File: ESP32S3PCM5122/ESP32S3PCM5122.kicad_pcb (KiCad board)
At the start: 2 copper layers, 84 x 70 mm, 28 parts, among them IC1 ESP32-S3-WROOM-1U-N16R8, IC2 AP63203, IC4 USBLC6, J1 OUT, J2 VOL, J5 PWR SW, J6 PWR LED, J7 USB IN, U1 PCM5122PW

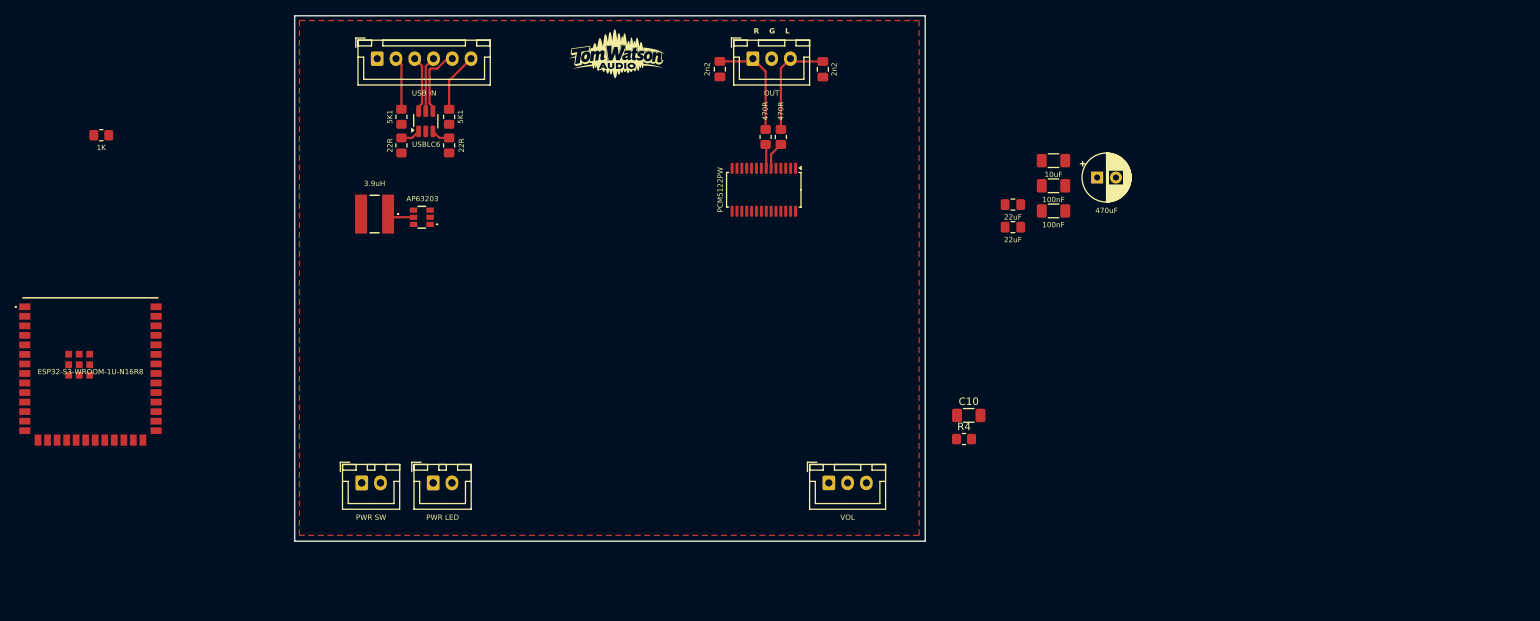
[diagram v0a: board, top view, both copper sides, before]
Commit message: move to PCM5242
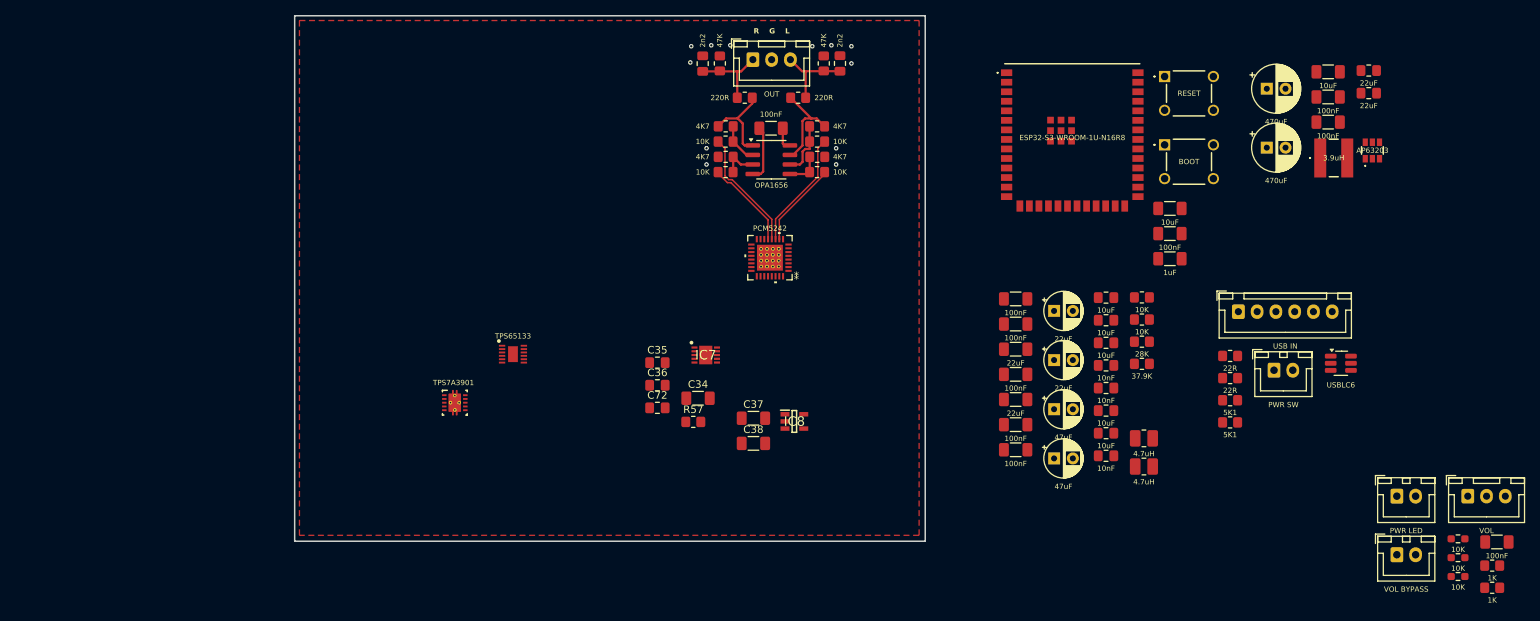
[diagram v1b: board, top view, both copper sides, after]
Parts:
- removed G***: LOGO, Custom:LOGONEW
- added C11: 10uF, Capacitor_SMD:C_1206_3216Metric_Pad1.33x1.80mm_HandSolder, F.Cu at (209.3, 104.4)
- added C12: 100nF, Capacitor_SMD:C_1206_3216Metric_Pad1.33x1.80mm_HandSolder, F.Cu at (209.3, 107.8)
- added C13: 1uF, Capacitor_SMD:C_1206_3216Metric_Pad1.33x1.80mm_HandSolder, F.Cu at (209.3, 111.1)
- added C14: 100nF, Capacitor_SMD:C_1206_3216Metric_Pad1.33x1.80mm_HandSolder, F.Cu at (188.8, 116.5)
- added C15: 10uF, Capacitor_SMD:C_0805_2012Metric_Pad1.18x1.45mm_HandSolder, F.Cu at (200.8, 122.3)
- added C16: 10nF, Capacitor_SMD:C_0805_2012Metric_Pad1.18x1.45mm_HandSolder, F.Cu at (200.8, 125.3)
- added C17: 10nF, Capacitor_SMD:C_0805_2012Metric_Pad1.18x1.45mm_HandSolder, F.Cu at (200.8, 128.3)
- added C18: 10uF, Capacitor_SMD:C_0805_2012Metric_Pad1.18x1.45mm_HandSolder, F.Cu at (200.8, 131.3)
- added C19: 10uF, Capacitor_SMD:C_0805_2012Metric_Pad1.18x1.45mm_HandSolder, F.Cu at (200.8, 134.3)
- added C20: 100nF, Capacitor_SMD:C_1206_3216Metric_Pad1.33x1.80mm_HandSolder, F.Cu at (188.8, 119.8)
- added C21: 22uF, Capacitor_SMD:C_1206_3216Metric_Pad1.33x1.80mm_HandSolder, F.Cu at (188.8, 123.2)
- added C22: 100nF, Capacitor_SMD:C_1206_3216Metric_Pad1.33x1.80mm_HandSolder, F.Cu at (188.8, 126.5)
- added C23: 22uF, Capacitor_SMD:C_1206_3216Metric_Pad1.33x1.80mm_HandSolder, F.Cu at (188.8, 129.9)
- added C24: 100nF, Capacitor_SMD:C_1206_3216Metric_Pad1.33x1.80mm_HandSolder, F.Cu at (188.8, 133.2)
- added C25: 100nF, Capacitor_SMD:C_1206_3216Metric_Pad1.33x1.80mm_HandSolder, F.Cu at (188.8, 136.6)
- added C26: 100nF, Capacitor_SMD:C_1206_3216Metric_Pad1.33x1.80mm_HandSolder, F.Cu at (156.2, 93.7)
- added C27: 22uF, Capacitor_THT:CP_Radial_D5.0mm_P2.50mm, F.Cu at (193.9, 118.1)
- added C28: 22uF, Capacitor_THT:CP_Radial_D5.0mm_P2.50mm, F.Cu at (193.9, 124.6)
- added C29: 47uF, Capacitor_THT:CP_Radial_D5.0mm_P2.50mm, F.Cu at (193.9, 131.2)
- added C30: 47uF, Capacitor_THT:CP_Radial_D5.0mm_P2.50mm, F.Cu at (193.9, 137.7)
- added C31: 10nF, Capacitor_SMD:C_0805_2012Metric_Pad1.18x1.45mm_HandSolder, F.Cu at (200.8, 137.4)
- added C32: 2n2, Capacitor_SMD:C_0805_2012Metric_Pad1.18x1.45mm_HandSolder, F.Cu at (165.4, 85.1)
- added C33: 2n2, Capacitor_SMD:C_0805_2012Metric_Pad1.18x1.45mm_HandSolder, F.Cu at (147.1, 85.1)
- added C34: 22uF, Capacitor_SMD:C_1206_3216Metric_Pad1.33x1.80mm_HandSolder, F.Cu at (146.4, 129.7)
- added C35: 10uF, Capacitor_SMD:C_0805_2012Metric_Pad1.18x1.45mm_HandSolder, F.Cu at (141.0, 125.0)
- added C36: 10uF, Capacitor_SMD:C_0805_2012Metric_Pad1.18x1.45mm_HandSolder, F.Cu at (141.0, 128.0)
- added C37: 1uF, Capacitor_SMD:C_1206_3216Metric_Pad1.33x1.80mm_HandSolder, F.Cu at (153.8, 132.4)
- added C38: 1uF, Capacitor_SMD:C_1206_3216Metric_Pad1.33x1.80mm_HandSolder, F.Cu at (153.8, 135.7)
- added C4: 470uF, Capacitor_THT:CP_Radial_D6.3mm_P2.50mm, F.Cu at (222.2, 96.3)
- added C72: 10nF, Capacitor_SMD:C_0805_2012Metric_Pad1.18x1.45mm_HandSolder, F.Cu at (141.0, 131.0)
- added IC3: RESET, Custom:TS026650BK100SCRD, F.Cu at (208.6, 86.8)
- added IC5: BOOT, Custom:TS026650BK100SCRD, F.Cu at (208.6, 95.9)
- added IC6: TPS65133, Custom:SON45P300X300X80-13N-D, F.Cu at (121.8, 123.8)
- added IC7: LT3042, Custom:LT3042, F.Cu at (147.5, 123.9)
- added IC8: TPS7A2033PDBVR, Custom:SOT95P280X145-5N, F.Cu at (159.3, 132.8)
- added J8: VOL BYPASS, Connector_JST:JST_XH_B2B-XH-A_1x02_P2.50mm_Vertical, F.Cu at (239.5, 150.5)
- added L2: 4.7uH, Inductor_SMD:L_1008_2520Metric_Pad1.43x2.20mm_HandSolder, F.Cu at (205.8, 135.0)
- added L3: 4.7uH, Inductor_SMD:L_1008_2520Metric_Pad1.43x2.20mm_HandSolder, F.Cu at (205.8, 138.8)
- added R10: 220R, Resistor_SMD:R_0805_2012Metric_Pad1.20x1.40mm_HandSolder, F.Cu at (159.8, 89.7)
- added R11: 220R, Resistor_SMD:R_0805_2012Metric_Pad1.20x1.40mm_HandSolder, F.Cu at (152.7, 89.7)
- added R14: 10K, Resistor_SMD:R_0805_2012Metric_Pad1.20x1.40mm_HandSolder, F.Cu at (162.3, 99.6)
- added R15: 10K, Resistor_SMD:R_0805_2012Metric_Pad1.20x1.40mm_HandSolder, F.Cu at (150.1, 99.6)
- added R16: 10K, Resistor_SMD:R_0805_2012Metric_Pad1.20x1.40mm_HandSolder, F.Cu at (162.3, 95.5)
- added R19: 10K, Resistor_SMD:R_0805_2012Metric_Pad1.20x1.40mm_HandSolder, F.Cu at (150.1, 95.5)
- added R20: 4K7, Resistor_SMD:R_0805_2012Metric_Pad1.20x1.40mm_HandSolder, F.Cu at (162.3, 97.5)
- added R21: 4K7, Resistor_SMD:R_0805_2012Metric_Pad1.20x1.40mm_HandSolder, F.Cu at (150.1, 97.5)
- added R22: 4K7, Resistor_SMD:R_0805_2012Metric_Pad1.20x1.40mm_HandSolder, F.Cu at (150.1, 93.5)
- added R23: 4K7, Resistor_SMD:R_0805_2012Metric_Pad1.20x1.40mm_HandSolder, F.Cu at (162.3, 93.5)
- added R24: 47K, Resistor_SMD:R_0805_2012Metric_Pad1.20x1.40mm_HandSolder, F.Cu at (163.2, 85.1)
- added R25: 47K, Resistor_SMD:R_0805_2012Metric_Pad1.20x1.40mm_HandSolder, F.Cu at (149.4, 85.1)
- added R5: 10K, Resistor_SMD:R_0603_1608Metric_Pad0.98x0.95mm_HandSolder, F.Cu at (247.7, 148.4)
- added R57: 33K2, Resistor_SMD:R_0805_2012Metric_Pad1.20x1.40mm_HandSolder, F.Cu at (145.8, 132.8)
- added R6: 10K, Resistor_SMD:R_0603_1608Metric_Pad0.98x0.95mm_HandSolder, F.Cu at (247.7, 150.9)
- added R7: 10K, Resistor_SMD:R_0603_1608Metric_Pad0.98x0.95mm_HandSolder, F.Cu at (247.7, 153.4)
- added R8: 28K, Resistor_SMD:R_0805_2012Metric_Pad1.20x1.40mm_HandSolder, F.Cu at (205.6, 122.2)
- added R9: 37.9K, Resistor_SMD:R_0805_2012Metric_Pad1.20x1.40mm_HandSolder, F.Cu at (205.6, 125.1)
- added U2: PCM5242, Custom:PCM5242, F.Cu at (156.0, 111.0)
- added U3: OPA1656, Package_SO:SOIC-8_3.9x4.9mm_P1.27mm, F.Cu at (156.2, 97.9)
- C2, C3: value 2n2 -> 10uF
- R1, R2: value 470R -> 10K
- U1: value PCM5122PW -> TPS7A3901; footprint Package_SO:TSSOP-28_4.4x9.7mm_P0.65mm -> Custom:TPS7A3901DSCR
- moved R3 194.0 mm to (252.2, 152.0)
- moved IC1 134.5 mm to (196.3, 94.7)
- moved J6 128.4 mm to (239.5, 142.7)
- moved L1 128.0 mm to (231.1, 97.7), turned to 0 degrees
- moved IC2 126.9 mm to (236.3, 96.7), turned to 0 degrees
- moved IC4 126.1 mm to (232.1, 125.0), turned to 0 degrees
- moved J5 122.5 mm to (223.2, 126.0)
- moved J7 119.6 mm to (218.4, 118.2)
- moved R18 117.7 mm to (217.3, 132.9), turned to 0 degrees
- moved R12 113.9 mm to (217.3, 124.1), turned to 0 degrees
- moved R17 110.7 mm to (217.3, 130.0), turned to 0 degrees
- moved R13 108.6 mm to (217.3, 127.0), turned to 0 degrees
- moved J2 85.1 mm to (249.0, 142.7)
- moved R4 73.1 mm to (252.2, 154.9)
- moved C10 72.4 mm to (252.9, 148.8)
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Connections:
- C1 pad 1: /5V IN -> VBUS
- C2 pad 1: Net-(J1-Pin_1) -> /OPA1656-POWER/VPOS
- C3 pad 1: Net-(J1-Pin_3) -> /OPA1656-POWER/VNEG
- C5 pad 2: /5V IN -> VBUS
- C6 pad 2: /5V IN -> VBUS
- C8 pad 1: /3V3DIG -> ESP3V3
- C9 pad 1: /3V3DIG -> ESP3V3
- IC1 pad 13: /D- -> /ESP32/D-
- IC1 pad 14: /D+ -> /ESP32/D+
- IC1 pad 2: /3V3DIG -> /ESP32/3V3DIG
- IC1 pad 27: unconnected-(IC1-IO0-Pad27) -> /ESP32/GPIO0
- IC1 pad 3: unconnected-(IC1-EN-Pad3) -> /ESP32/EN
- IC2 pad 1: /3V3DIG -> ESP3V3
- IC2 pad 2: /5V IN -> VBUS
- IC2 pad 3: /5V IN -> VBUS
- J5 pad 1: /5V IN -> Net-(IC4-VBUS)
- J5 pad 2: unconnected-(J5-Pin_2-Pad2) -> VBUS
- L1 pad 2: /3V3DIG -> ESP3V3
- R1 pad 1: Net-(U1-OUTL) -> Net-(U1-OUTP)
- R1 pad 2: Net-(J1-Pin_3) -> Net-(U1-FBP)
- R12 pad 1: /D- -> D+
- R13 pad 1: /D+ -> D-
- R2 pad 2: Net-(J1-Pin_1) -> Net-(U1-BUF)
- U1 pad 1: unconnected-(U1-CPVDD-Pad1) -> /OPA1656-POWER/VPOS
- U1 pad 10: unconnected-(U1-VCOM/DEMP-Pad10) -> Net-(U1-OUTP)
- U1 pad 11: unconnected-(U1-SDA/MOSI/ATT2-Pad11) -> GND
- U1 pad 2: unconnected-(U1-CAPP-Pad2) -> /OPA1656-POWER/VPOS
- U1 pad 3: GND -> Net-(U1-NR_SS)
- U1 pad 4: unconnected-(U1-CAPM-Pad4) -> GND
- U1 pad 5: unconnected-(U1-VNEG-Pad5) -> /OPA1656-POWER/VNEG
- U1 pad 6: Net-(U1-OUTL) -> Net-(U1-OUTN)
- U1 pad 8: unconnected-(U1-AVDD-Pad8) -> Net-(U1-BUF)
- U1 pad 9: GND -> Net-(U1-FBP)
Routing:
- net Net-(U2-OUTRN): track 0.00 -> 16.2 mm
- net Net-(U2-OUTLN): track 0.00 -> 15.7 mm
- net Net-(R10-Pad2): track 0.00 -> 13.2 mm
- net Net-(U2-OUTRP): track 0.00 -> 12.0 mm
- net Net-(R11-Pad2): track 0.00 -> 11.9 mm
- net Net-(U2-OUTLP): track 0.00 -> 11.4 mm
- net Net-(IC4-I/O2_2): track 9.34 -> 0.00 mm
- net Net-(J7-Pin_6): track 7.96 -> 0.00 mm
- net Net-(IC4-I/O1_2): track 7.57 -> 0.00 mm
- net Net-(U1-OUTN): track 0.00 -> 7.43 mm
- net Net-(IC4-VBUS): track 7.41 -> 0.00 mm
- net Net-(U3B--): track 0.00 -> 7.29 mm
- net Net-(J7-Pin_2): track 7.07 -> 0.00 mm
- net Net-(U3A-+): track 0.00 -> 5.96 mm
- net Net-(U3A--): track 0.00 -> 5.40 mm
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- added copper zone on In1.Cu, net GND
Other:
- copper layers 2 -> 4

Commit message: more work
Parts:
- removed C22, C24, C25, C26: 100nF, Capacitor_SMD:C_1206_3216Metric_Pad1.33x1.80mm_HandSolder
- removed C23: 22uF, Capacitor_SMD:C_1206_3216Metric_Pad1.33x1.80mm_HandSolder
- removed C27, C28: 22uF, Capacitor_THT:CP_Radial_D5.0mm_P2.50mm
- removed C29, C30: 47uF, Capacitor_THT:CP_Radial_D5.0mm_P2.50mm
- removed C31: 10nF, Capacitor_SMD:C_0805_2012Metric_Pad1.18x1.45mm_HandSolder
- removed IC6: TPS65133, Custom:SON45P300X300X80-13N-D
- removed L2, L3: 4.7uH, Inductor_SMD:L_1008_2520Metric_Pad1.43x2.20mm_HandSolder
- removed R1, R2: 10K, Resistor_SMD:R_0805_2012Metric_Pad1.20x1.40mm_HandSolder
- removed R8: 28K, Resistor_SMD:R_0805_2012Metric_Pad1.20x1.40mm_HandSolder
- removed R9: 37.9K, Resistor_SMD:R_0805_2012Metric_Pad1.20x1.40mm_HandSolder
- removed U1: TPS7A3901, Custom:TPS7A3901DSCR
- added G***: LOGO, Custom:LOGONEW, F.Cu at (135.1, 84.5)
- added PS1: LM27762, Custom:LM27762DSSR, F.Cu at (135.2, 95.9)
- C15, C2, C3: value 10uF -> 100nF; footprint Capacitor_SMD:C_0805_2012Metric_Pad1.18x1.45mm_HandSolder -> Capacitor_SMD:C_1206_3216Metric_Pad1.33x1.80mm_HandSolder
- C16: value 10nF -> 2.2uF
- C17: value 10nF -> 10uF
- C20: value 100nF -> 2.2uF; footprint Capacitor_SMD:C_1206_3216Metric_Pad1.33x1.80mm_HandSolder -> Capacitor_SMD:C_0805_2012Metric_Pad1.18x1.45mm_HandSolder
- C21: value 22uF -> 1uF
- IC8: value TPS7A2033PDBVR -> TPS7A2033
- moved J5 154.9 mm to (70.1, 102.1)
- moved IC4 125.9 mm to (110.6, 92.1), turned to 90 degrees
- moved R18 119.9 mm to (104.9, 91.2), turned to -90 degrees
- moved L1 119.6 mm to (112.0, 108.7)
- moved IC2 119.6 mm to (117.2, 107.7)
- moved J7 118.8 mm to (104.5, 84.6)
- moved R12 114.9 mm to (107.2, 91.2), turned to 90 degrees
- moved R13 109.5 mm to (113.8, 91.2), turned to 90 degrees
- moved R17 108.4 mm to (116.1, 91.2), turned to -90 degrees
- moved IC1 89.9 mm to (111.0, 123.3), turned to -90 degrees
- moved C19 59.7 mm to (150.1, 102.7), turned to 180 degrees
- moved C4 52.2 mm to (184.2, 132.1)
- moved C2 49.8 mm to (156.3, 93.9)
- moved C21 44.3 mm to (147.8, 106.3), turned to 180 degrees
- moved C16 43.7 mm to (160.4, 108.7), turned to 90 degrees
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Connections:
- C1 pad 1: VBUS -> /DAC-POWER/VBUS
- C11 pad 2: /ESP32/3V3DIG -> /ES32-POWER/ESP3V3
- C12 pad 2: /ESP32/3V3DIG -> /ES32-POWER/ESP3V3
- C14 pad 1: /OPA1656-POWER/PVIN -> /DAC-POWER/DAC3V3ANA
- C15 pad 1: /OPA1656-POWER/PVIN -> /DAC-POWER/DAC3V3DIG
- C16 pad 1: Net-(U1-OUTP) -> Net-(U2-CAPP)
- C16 pad 2: Net-(U1-FBP) -> Net-(U2-CAPM)
- C17 pad 1: Net-(U1-FBN) -> /DAC-POWER/DAC3V3ANA
- C17 pad 2: Net-(U1-OUTN) -> GND
- C18 pad 1: Net-(U1-OUTP) -> /DAC-POWER/DAC3V3DIG
- C19 pad 1: GND -> /DAC-POWER/DAC3V3ANA
- C19 pad 2: Net-(U1-OUTN) -> GND
- C2 pad 1: /OPA1656-POWER/VPOS -> Net-(PS1-OUT+)
- C2 pad 2: GND -> Net-(PS1-OUT-)
- C20 pad 1: /OPA1656-POWER/VPOS -> Net-(U2-VNEG)
- C21 pad 1: /OPA1656-POWER/VNEG -> Net-(U2-VCOM)
- C3 pad 1: /OPA1656-POWER/VNEG -> /DAC-POWER/DAC3V3ANA
- C34 pad 1: Net-(IC7-EN/UV) -> /DAC-POWER/VBUS
- C35 pad 2: Net-(IC7-EN/UV) -> /DAC-POWER/VBUS
- C36 pad 1: Net-(IC7-OUT) -> /DAC-POWER/DAC3V3ANA
- C37 pad 1: Net-(IC8-EN) -> /DAC-POWER/VBUS
- C38 pad 1: Net-(IC8-OUT) -> /DAC-POWER/DAC3V3DIG
- C4 pad 1: ESP3V3 -> /ES32-POWER/ESP3V3
- C5 pad 2: VBUS -> /DAC-POWER/VBUS
- C6 pad 2: VBUS -> /DAC-POWER/VBUS
- C8 pad 1: ESP3V3 -> /ES32-POWER/ESP3V3
- C9 pad 1: ESP3V3 -> /ES32-POWER/ESP3V3
- IC1 pad 2: /ESP32/3V3DIG -> /ES32-POWER/ESP3V3
- IC2 pad 1: ESP3V3 -> /ES32-POWER/ESP3V3
- IC2 pad 2: VBUS -> /DAC-POWER/VBUS
- IC2 pad 3: VBUS -> /DAC-POWER/VBUS
- IC7 pad 1: Net-(IC7-EN/UV) -> /DAC-POWER/VBUS
- IC7 pad 10: Net-(IC7-OUT) -> /DAC-POWER/DAC3V3ANA
- IC7 pad 2: Net-(IC7-EN/UV) -> /DAC-POWER/VBUS
- IC7 pad 3: Net-(IC7-EN/UV) -> /DAC-POWER/VBUS
- IC7 pad 6: Net-(IC7-EN/UV) -> /DAC-POWER/VBUS
- IC7 pad 9: Net-(IC7-OUT) -> /DAC-POWER/DAC3V3ANA
- IC8 pad 1: Net-(IC8-EN) -> /DAC-POWER/VBUS
- IC8 pad 3: Net-(IC8-EN) -> /DAC-POWER/VBUS
- IC8 pad 5: Net-(IC8-OUT) -> /DAC-POWER/DAC3V3DIG
- J5 pad 2: VBUS -> /DAC-POWER/VBUS
- L1 pad 2: ESP3V3 -> /ES32-POWER/ESP3V3
- R12 pad 1: D+ -> /ESP32/D+
- R13 pad 1: D- -> /ESP32/D-
- U2 pad 14: unconnected-(U2-AVDD-Pad14) -> /DAC-POWER/DAC3V3ANA
- U2 pad 16: unconnected-(U2-VCOM-Pad16) -> Net-(U2-VCOM)
- U2 pad 17: unconnected-(U2-SDA-Pad17) -> /DAC/SDA
- U2 pad 18: unconnected-(U2-SCL-Pad18) -> /DAC/SCL
- U2 pad 23: unconnected-(U2-MODE1-Pad23) -> GND
- U2 pad 24: unconnected-(U2-MODE2-Pad24) -> /DAC-POWER/DAC3V3DIG
- U2 pad 26: unconnected-(U2-SCK-Pad26) -> /DAC/SCK
- U2 pad 27: unconnected-(U2-BCK-Pad27) -> /DAC/BCK
- U2 pad 28: unconnected-(U2-DIN-Pad28) -> /DAC/DATA
- U2 pad 31: unconnected-(U2-LRCK-Pad31) -> /DAC/LRCK
- U2 pad 4: unconnected-(U2-DVDD-Pad4) -> /DAC-POWER/DAC3V3DIG
- U2 pad 5: unconnected-(U2-CPVDD-Pad5) -> /DAC-POWER/DAC3V3ANA
- U2 pad 6: unconnected-(U2-CAPP-Pad6) -> Net-(U2-CAPP)
- U2 pad 7: unconnected-(U2-CPGND-Pad7) -> GND
- U2 pad 8: unconnected-(U2-CAPM-Pad8) -> Net-(U2-CAPM)
- U2 pad 9: unconnected-(U2-VNEG-Pad9) -> Net-(U2-VNEG)
- U2 pad V: (no net) -> GND
- U3 pad 4: Net-(U1-OUTN) -> Net-(PS1-OUT+)
- U3 pad 8: Net-(U1-OUTP) -> Net-(PS1-OUT-)
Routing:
- net /DAC-POWER/DAC3V3ANA: track 0.00 -> 48.7 mm, vias 0 -> 3
- net /DAC-POWER/VBUS: track 0.00 -> 35.5 mm, vias 0 -> 2
- net /ESP32/D-: track 0.00 -> 27.0 mm
- net /ESP32/D+: track 0.00 -> 24.1 mm
- net GND: track 0.00 -> 24.0 mm
- net /DAC-POWER/DAC3V3DIG: track 0.00 -> 22.4 mm, vias 0 -> 2
- net Net-(IC4-I/O2_2): track 0.00 -> 7.43 mm
- net Net-(U1-OUTN): track 7.43 -> 0.00 mm
- net Net-(PS1-OUT+): track 0.00 -> 7.43 mm
- net Net-(IC4-VBUS): track 0.00 -> 6.79 mm
- net Net-(J7-Pin_2): track 0.00 -> 6.46 mm
- net Net-(IC7-SET): track 0.00 -> 6.40 mm
- net Net-(IC4-I/O1_2): track 0.00 -> 6.26 mm
- net Net-(U2-VCOM): track 0.00 -> 6.18 mm
- net Net-(J7-Pin_6): track 0.00 -> 5.98 mm
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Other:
- board text added: "GND CC1 D+ 5V D- CC2"
- board text added: "PortaDAC"
- board text added: "Reference"
- board text added: "Series"

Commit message: more work
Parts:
- added C10: 100nF, Capacitor_SMD:C_1206_3216Metric_Pad1.33x1.80mm_HandSolder, F.Cu at (166.6, 134.4)
- added R1: 10K, Resistor_SMD:R_0603_1608Metric_Pad0.98x0.95mm_HandSolder, F.Cu at (136.1, 125.7)
- added R2: 10K, Resistor_SMD:R_0603_1608Metric_Pad0.98x0.95mm_HandSolder, F.Cu at (133.3, 134.5)
- added R4: 1K, Resistor_SMD:R_0805_2012Metric_Pad1.20x1.40mm_HandSolder, F.Cu at (162.6, 135.1)
- moved C8 120.5 mm to (118.9, 115.1)
- moved C9 120.2 mm to (118.9, 117.1)
- moved C7 117.4 mm to (113.7, 106.7), turned to 180 degrees
- moved C5 109.4 mm to (124.2, 112.8), turned to 180 degrees
- moved C6 108.2 mm to (124.2, 110.5), turned to 180 degrees
- moved C12 95.4 mm to (114.3, 116.8)
- moved IC3 92.3 mm to (124.3, 124.2)
- moved IC5 92.0 mm to (124.2, 132.6)
- moved J2 88.9 mm to (160.1, 142.2)
- moved C4 80.3 mm to (105.7, 115.1), turned to 180 degrees
- moved J5 77.1 mm to (135.9, 142.2)
- moved C13 76.8 mm to (134.1, 126.5), turned to -90 degrees
- moved IC1 6.86 mm to (110.7, 130.1)
- moved IC2 4.71 mm to (118.9, 112.1)
- moved L1 3.08 mm to (112.5, 111.8), turned to 180 degrees
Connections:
- J2 pad 1: /3V3DIG -> /ES32-POWER/ESP3V3
- U2 pad V: GND -> (no net)
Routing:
- net /ES32-POWER/ESP3V3: track 0.00 -> 129.5 mm, vias 0 -> 3
- net Net-(IC4-VBUS): track 6.79 -> 130.3 mm
- net /DAC-POWER/VBUS: track 35.5 -> 141.4 mm, vias 2 -> 5
- net Net-(PS1-OUT-): track 3.15 -> 47.8 mm, vias 0 -> 2
- net /ESP32/GPIO0: track 0.00 -> 36.6 mm, vias 0 -> 1
- net Net-(PS1-OUT+): track 7.43 -> 30.5 mm, vias 0 -> 2
- net /ESP32/EN: track 0.00 -> 22.6 mm, vias 0 -> 1
- net /DAC-POWER/DAC3V3DIG: track 22.4 -> 35.8 mm, vias 2 -> 3
- net Net-(IC2-SW): track 0.00 -> 12.0 mm
- net /ESP32/D-: track 27.0 -> 35.9 mm
- net /ESP32/D+: track 24.1 -> 32.4 mm
- net Net-(J2-Pin_2): track 0.00 -> 6.11 mm
- net Net-(IC2-BST): track 0.00 -> 5.68 mm
- net GND: track 24.0 -> 29.1 mm, vias 12 -> 94
- net Net-(C10-Pad2): track 0.00 -> 2.51 mm
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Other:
- board text added: "+ W G"
